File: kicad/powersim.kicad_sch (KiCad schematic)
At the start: 9 parts, among them J1 Bus_PCI_Express_x1, J2 Conn_01x02_Pin, J6 USB_C_Receptacle_USB2.0_16P, U1 AP63203WU

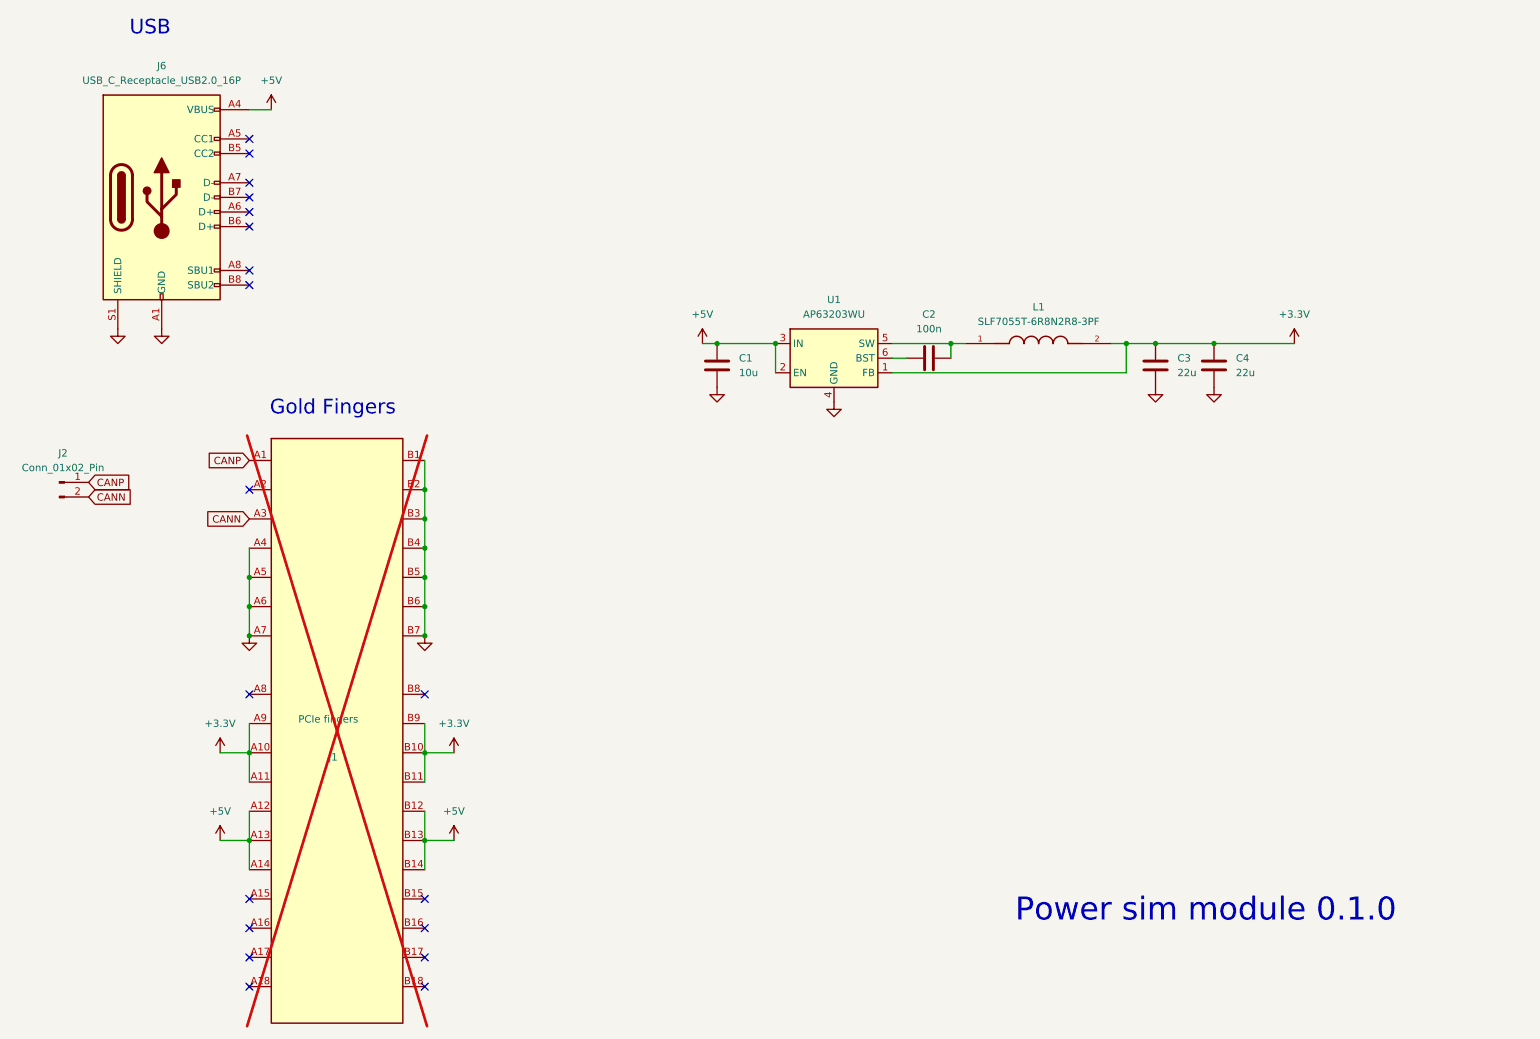
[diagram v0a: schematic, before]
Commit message: add test points and USB pull down resistors
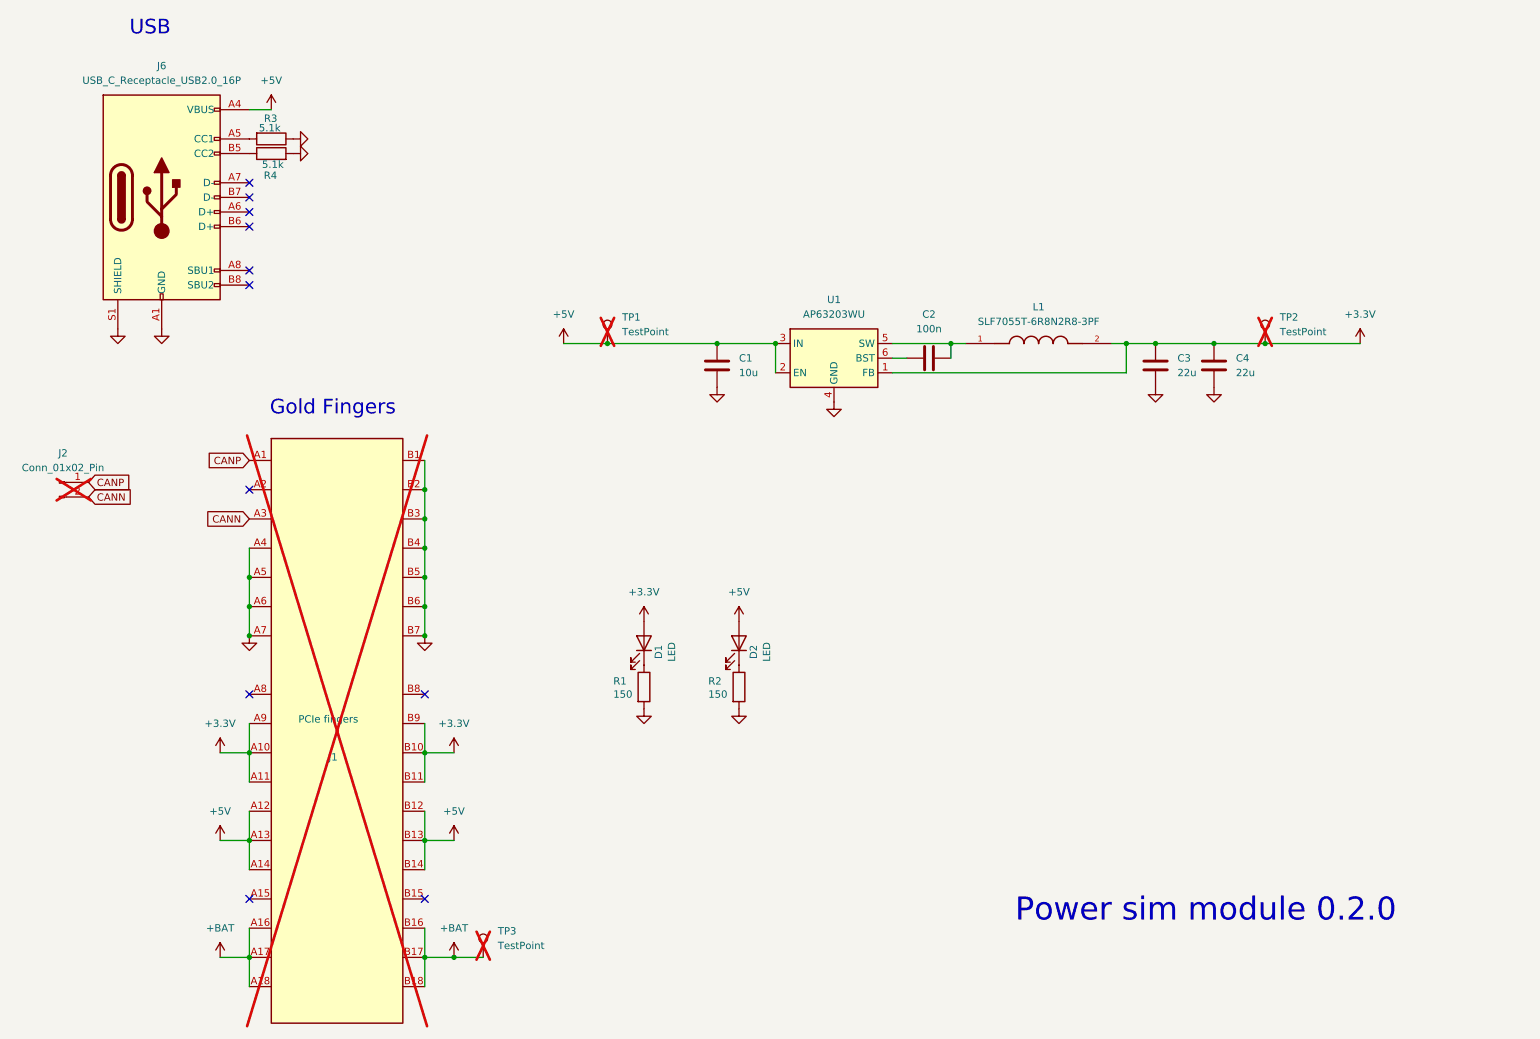
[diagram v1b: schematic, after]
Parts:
- added D1, D2: LED, LED_SMD:LED_0603_1608Metric, symbol Device:LED
- added R1, R2: 150, Resistor_SMD:R_0603_1608Metric, symbol Device:R
- added R3, R4: 5.1k, Resistor_SMD:R_0402_1005Metric, symbol Device:R
- added TP1, TP2, TP3: TestPoint, Connector_PinHeader_2.54mm:PinHeader_1x01_P2.54mm_Vertical, symbol Connector:TestPoint
- J2: now not fitted
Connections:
- net +3.3V: now also D1.2 (A), TP2.1
- net +5V: now also D2.2 (A), TP1.1
- net GND: now also R1.2, R2.2, R3.1, R4.2
- net +BAT: now reaches J1.A16 (PERp0)
- net +BAT: now also J1.A17 (PERn0), J1.A18 (GND), J1.B16 (GND), J1.B17 (~{PRSNT2}), J1.B18 (GND), TP3.1
- net at J6.A5 (CC1): now also R3.2
- net at J6.B5 (CC2): now also R4.1
- new net: D2.1 (K), R2.1
- new net: D1.1 (K), R1.1
- no-connect marks 19 -> 11
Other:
- note added: "Power sim module 0.2.0"
- note removed: "Power sim module 0.1.0"
